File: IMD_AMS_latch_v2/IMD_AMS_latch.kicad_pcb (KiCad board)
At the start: 2 copper layers, 66.9 x 59.9 mm, 43 parts, among them J10 Conn_01x02, J13 Conn_01x02, J2 Conn_01x02, J5 Conn_01x02, J6 Conn_01x02, J7 Conn_01x02, J8 Conn_01x02, J9 Conn_01x02, K1 SANYOU_SRD_Form_C, K2 SANYOU_SRD_Form_C, Q1 AO3400A, Q2 AO3400A, U1 MC14044BDR2G, U2 LM393

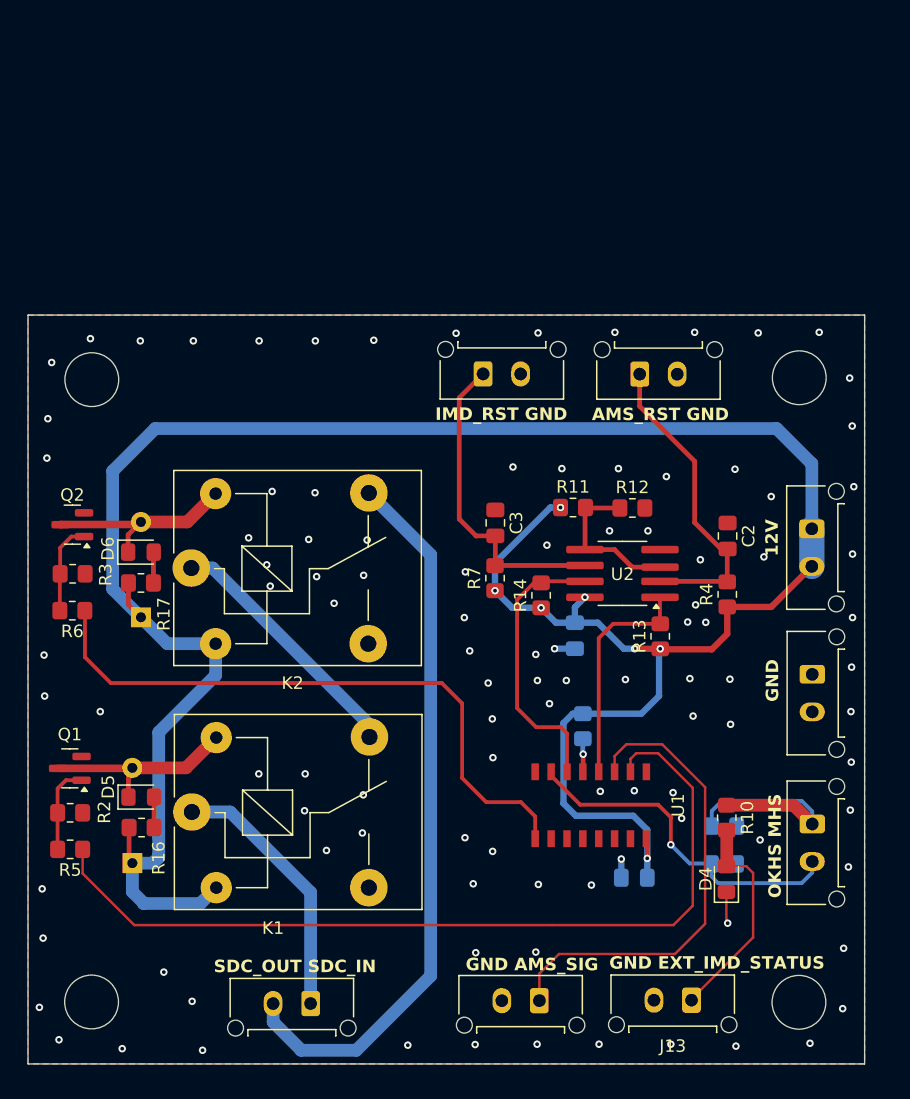
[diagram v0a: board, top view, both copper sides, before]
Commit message: changed to horizontal molex microfit
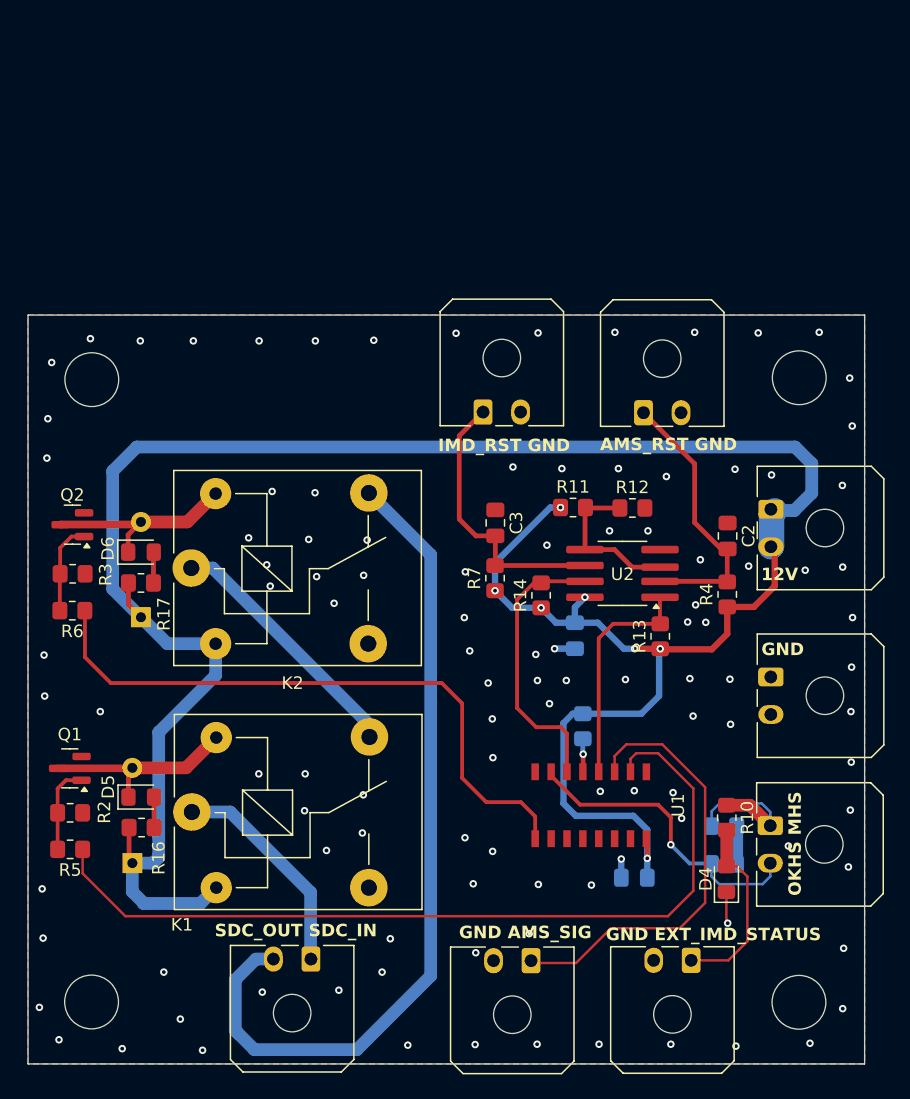
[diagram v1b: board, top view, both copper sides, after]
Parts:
- J10, J13, J2, J5, J6, J7, J8, J9: footprint Connector_Molex:Molex_Micro-Fit_3.0_43650-0215_1x02_P3.00mm_Vertical -> Connector_Molex:Molex_Micro-Fit_3.0_43650-0200_1x02_P3.00mm_Horizontal
- moved J2 3.63 mm to (189.3, 71.2)
- moved J7 3.56 mm to (152.5, 107.2)
- moved J8 3.36 mm to (189.2, 96.5)
- moved J6 3.31 mm to (189.3, 84.7)
- moved J5 3.26 mm to (170.1, 107.3)
- moved J13 3.18 mm to (182.9, 107.3)
- moved J9 3.10 mm to (179.1, 63.5)
- moved J10 3.05 mm to (166.2, 63.5)
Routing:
- net /SDC_OUT: track 58.1 -> 67.9 mm
- net /IMD_MHS: track 18.4 -> 11.9 mm
- net /SDC_IN: track 21.0 -> 17.5 mm
- net /IMD_OKHS: track 27.9 -> 24.6 mm
- net GND: track 5.67 -> 8.71 mm, vias 105 -> 110
- net /AMS_reset_btn: track 25.2 -> 22.3 mm
- net /IMD_reset_btn: track 25.4 -> 22.5 mm
- net /AMS_signal: track 38.3 -> 35.6 mm
- net Net-(D4-A): track 17.5 -> 15.2 mm
- net /AMS_latch: track 69.8 -> 68.6 mm
- net +12V: track 198.3 -> 197.2 mm

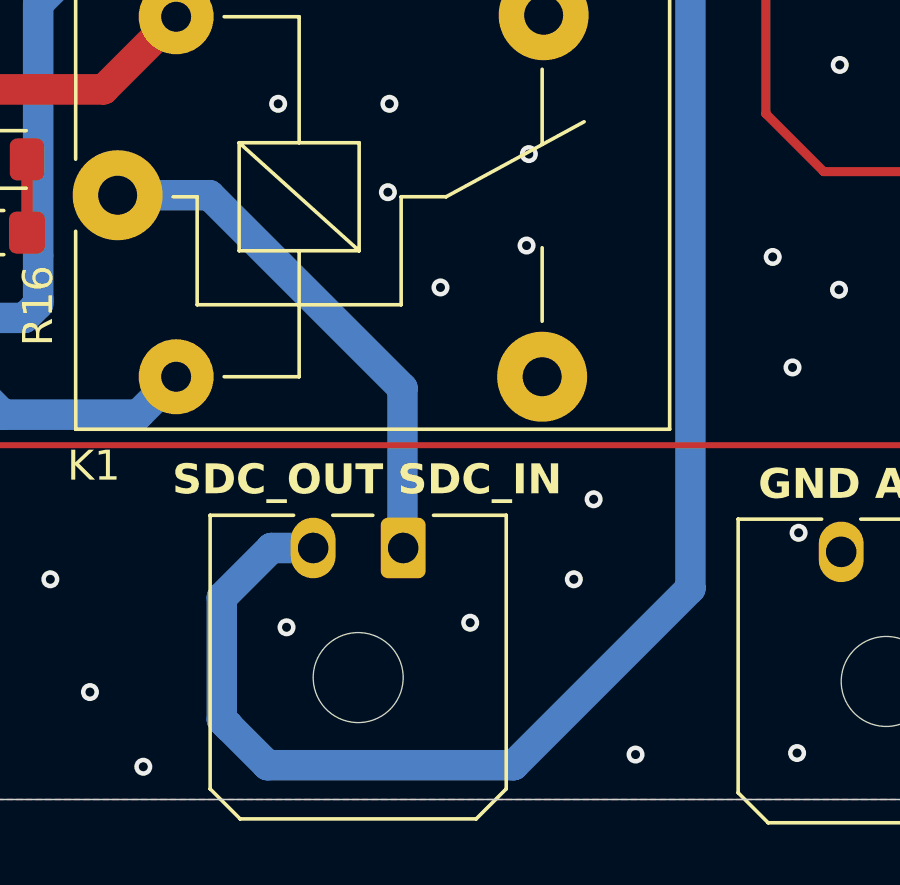
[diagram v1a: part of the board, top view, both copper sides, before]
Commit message: minor update on SDC IN & SDC out wiring
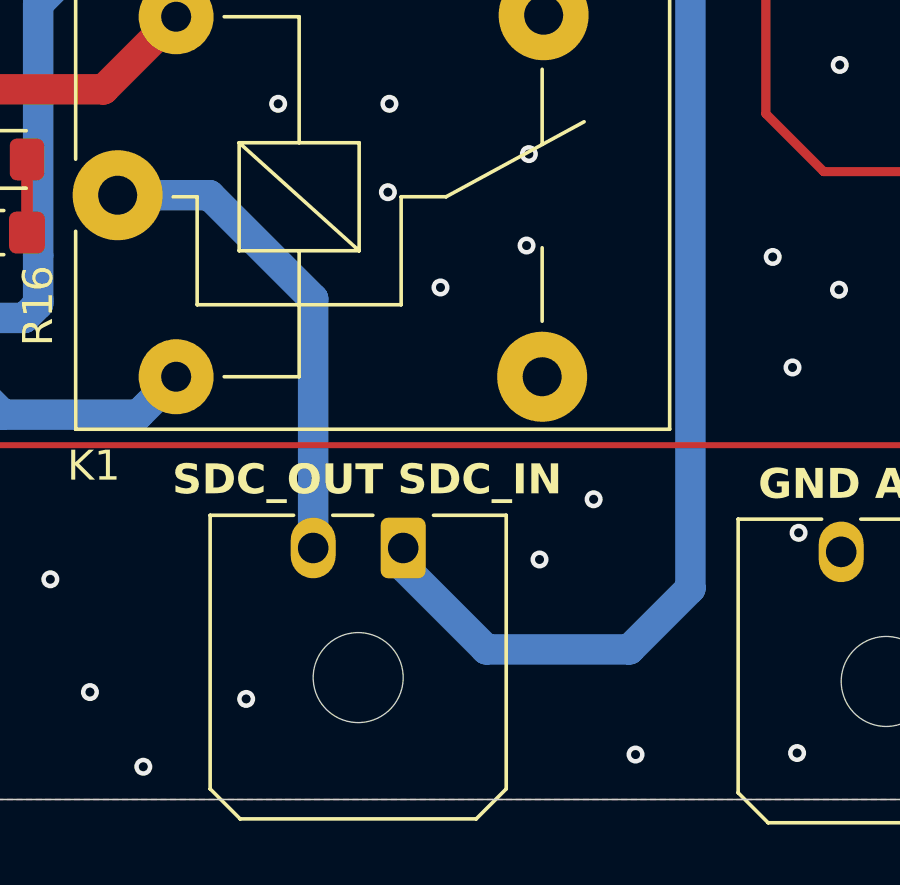
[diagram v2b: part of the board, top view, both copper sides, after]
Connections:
- J7 pad 1: /SDC_IN -> /SDC_OUT
- J7 pad 2: /SDC_OUT -> /SDC_IN
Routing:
- net /SDC_OUT: track 67.9 -> 52.9 mm
- net /SDC_IN: track 17.5 -> 16.9 mm
- net GND: vias 110 -> 109
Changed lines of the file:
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@@
 			(remove_unused_layers no)
 			(roundrect_rratio 0.166667)
-			(net 9 "/SDC_IN")
+			(net 10 "/SDC_OUT")
 			(pinfunction "Pin_1")
 			(pintype "passive")
@@
 			(layers "*.Cu" "*.Mask")
 			(remove_unused_layers no)
-			(net 10 "/SDC_OUT")
+			(net 9 "/SDC_IN")
 			(pinfunction "Pin_2")
 			(pintype "passive")
@@
 	)
 	(via
-		(at 148.59 109.855)
+		(at 147.2438 112.2426)
 		(size 0.6)
 		(drill 0.3)
@@
 	)
 	(via
-		(at 158.1658 108.2548)
+		(at 157.0228 107.5944)
 		(size 0.6)
 		(drill 0.3)
@@
 	)
 	(via
-		(at 154.7114 109.7026)
-		(size 0.6)
-		(drill 0.3)
-		(layers "F.Cu" "B.Cu")
-		(free yes)
-		(net 1)
-	)
-	(via
 		(at 184.0484 80.2894)
 		(size 0.6)
@@
 	)
 	(segment
-		(start 152.503 107.2114)
-		(end 152.4536 107.162)
+		(start 149.4776 98.9062)
+		(end 146.0246 95.4532)
 		(width 1.016)
 		(layer "B.Cu")
@@
 	)
 	(segment
-		(start 152.4536 107.162)
-		(end 152.4536 101.8822)
+		(start 149.4776 107.2114)
+		(end 149.4776 98.9062)
 		(width 1.016)
 		(layer "B.Cu")
@@
 	)
 	(segment
-		(start 152.4536 101.8822)
-		(end 146.0246 95.4532)
-		(width 1.016)
-		(layer "B.Cu")
-		(net 9)
-	)
-	(segment
-		(start 162.052 74.8886)
-		(end 162.052 108.5596)
-		(width 1.016)
-		(layer "B.Cu")
-		(net 10)
-	)
-	(segment
-		(start 148.084 107.2114)
-		(end 149.503 107.2114)
-		(width 1.016)
-		(layer "B.Cu")
-		(net 10)
-	)
-	(segment
-		(start 146.6469 113.1443)
-		(end 146.431 112.9284)
-		(width 1.016)
-		(layer "B.Cu")
-		(net 10)
-	)
-	(segment
 		(start 149.0692 107.6452)
 		(end 149.503 107.2114)
 		(width 0.2)
 		(layer "B.Cu")
-		(net 10)
+		(net 9)
 	)
 	(segment
-		(start 146.431 108.8644)
-		(end 148.084 107.2114)
+		(start 160.02 110.5916)
+		(end 155.249342 110.5916)
 		(width 1.016)
 		(layer "B.Cu")
@@
 	)
 	(segment
-		(start 147.955 114.4524)
-		(end 146.6469 113.1443)
+		(start 155.249342 110.5916)
+		(end 152.4776 107.819858)
 		(width 1.016)
 		(layer "B.Cu")
@@
 	)
 	(segment
-		(start 156.1592 114.4524)
-		(end 147.955 114.4524)
+		(start 152.503 107.2114)
+		(end 152.4536 107.162)
 		(width 1.016)
 		(layer "B.Cu")
@@
 	)
 	(segment
-		(start 157.1094 69.946)
-		(end 162.052 74.8886)
+		(start 162.052 74.8886)
+		(end 162.052 108.5596)
 		(width 1.016)
 		(layer "B.Cu")
@@
 	)
 	(segment
-		(start 146.6469 113.1443)
-		(end 146.558 113.0554)
+		(start 157.1094 69.946)
+		(end 162.052 74.8886)
 		(width 1.016)
 		(layer "B.Cu")
@@
 	)
 	(segment
-		(start 146.431 112.9284)
-		(end 146.431 108.8644)
+		(start 152.4776 107.819858)
+		(end 152.4776 107.2114)
 		(width 1.016)
 		(layer "B.Cu")
@@
 	(segment
 		(start 162.052 108.5596)
-		(end 156.1592 114.4524)
+		(end 160.02 110.5916)
 		(width 1.016)
 		(layer "B.Cu")
@@
 	)
 	(zone
-		(net 14)
-		(net_name "Net-(K1-Pad4)")
+		(net 23)
+		(net_name "Net-(U1-EN)")
 		(layer "B.Cu")
 		(name "$teardrop_padvia$")
 		(hatch full 0.1)
-		(priority 30001)
+		(priority 30002)
 		(attr
 			(teardrop
@@
 		(polygon
 			(pts
-				(xy 144.812131 76.848952) (xy 145.530552 76.130531) (xy 144.213691 75.230765) (xy 142.908693 75.945293)
-				(xy 143.752001 77.176756)
+				(xy 174.4091 90.236164) (xy 174.0281 90.236164) (xy 173.949764 90.771873) (xy 174.244 90.8314) (xy 174.538236 90.771873)
 			)
 		)
 	)
 	(zone
-		(net 23)
-		(net_name "Net-(U1-EN)")
+		(net 14)
+		(net_name "Net-(K1-Pad4)")
 		(layer "B.Cu")
 		(name "$teardrop_padvia$")
 		(hatch full 0.1)
-		(priority 30002)
+		(priority 30001)
 		(attr
 			(teardrop
@@
 		(polygon
 			(pts
-				(xy 174.4091 90.236164) (xy 174.0281 90.236164) (xy 173.949764 90.771873) (xy 174.244 90.8314) (xy 174.538236 90.771873)
+				(xy 144.812131 76.848952) (xy 145.530552 76.130531) (xy 144.213691 75.230765) (xy 142.908693 75.945293)
+				(xy 143.752001 77.176756)
 			)
 		)

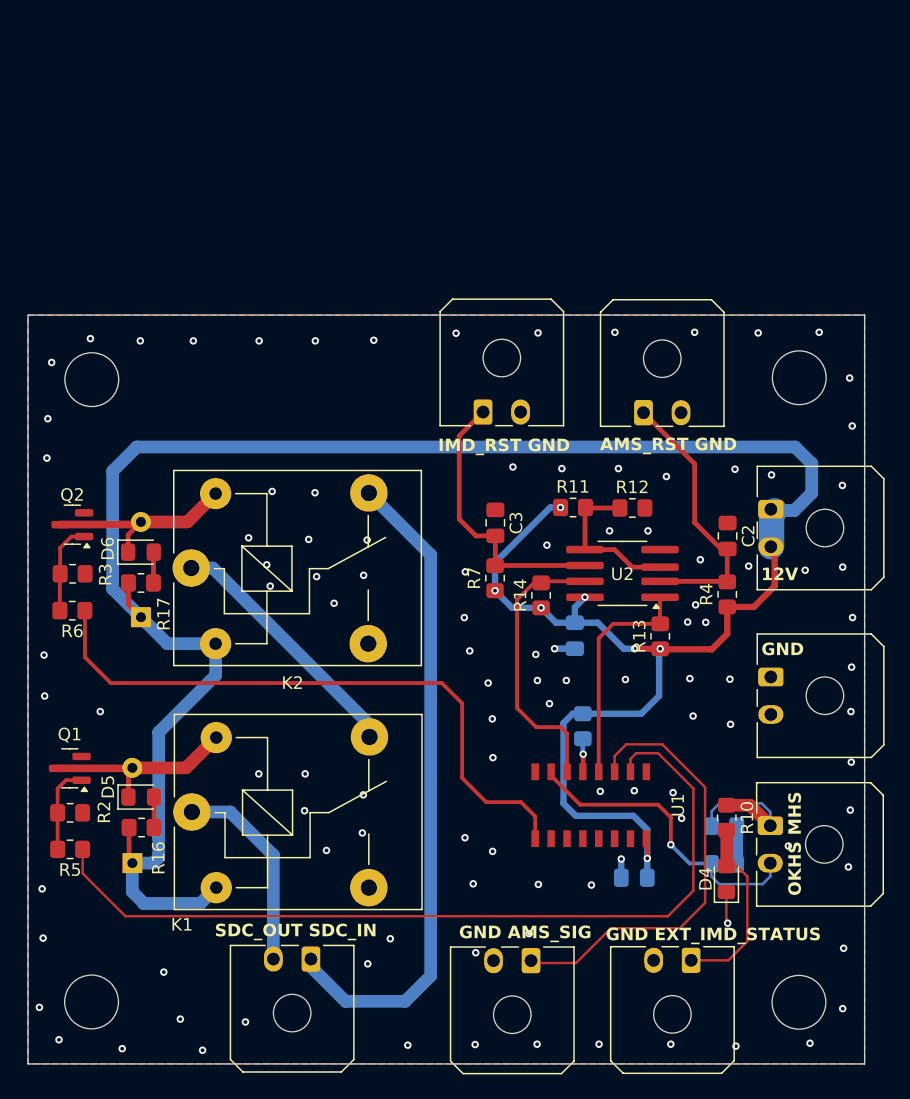
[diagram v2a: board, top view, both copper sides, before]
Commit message: fixed connectors
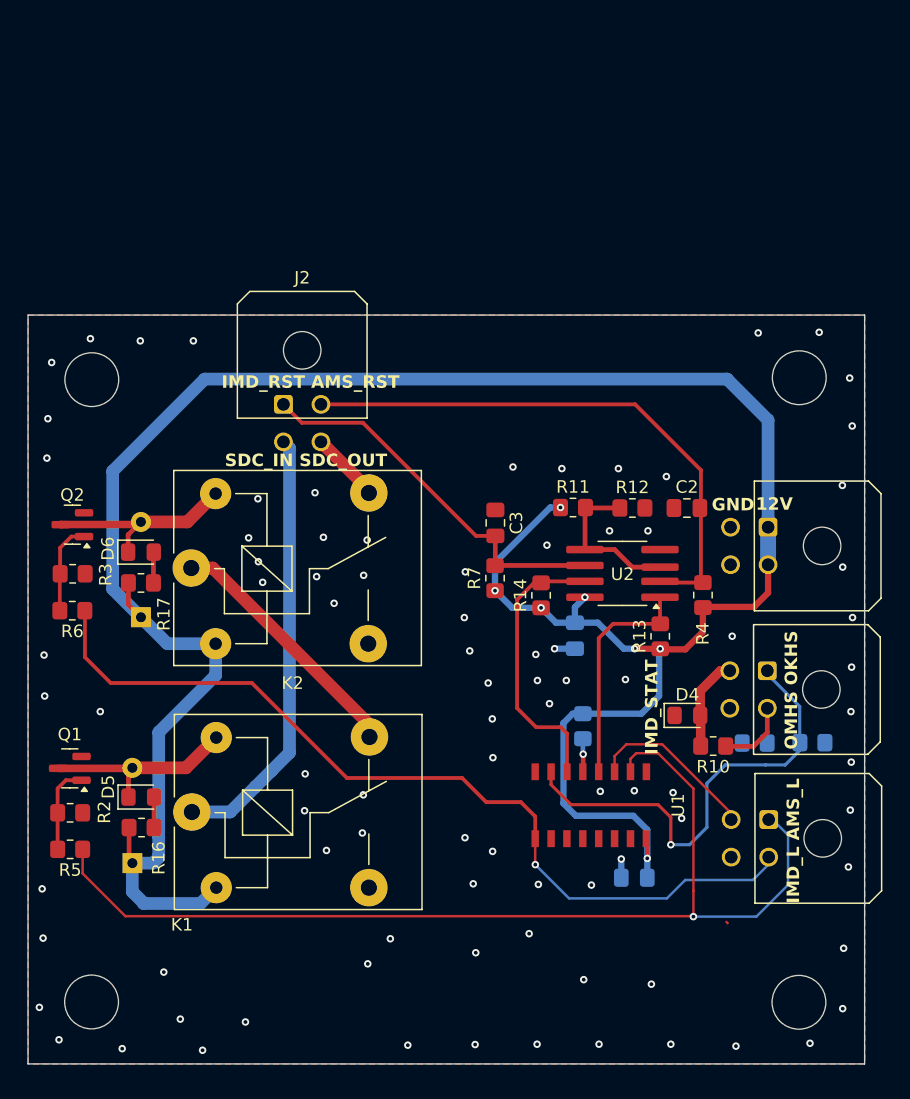
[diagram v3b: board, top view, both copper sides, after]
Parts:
- removed J10, J13, J5, J6, J7, J8, J9: Conn_01x02, Connector_Molex:Molex_Micro-Fit_3.0_43650-0200_1x02_P3.00mm_Horizontal
- added J1: Conn_01x04, Connector_Molex:Molex_Micro-Fit_3.0_43045-0400_2x02_P3.00mm_Horizontal, F.Cu at (189.1, 96.1)
- added J3: Conn_01x04, Connector_Molex:Molex_Micro-Fit_3.0_43045-0400_2x02_P3.00mm_Horizontal, F.Cu at (189.0, 84.2)
- added J4: Conn_01x04, Connector_Molex:Molex_Micro-Fit_3.0_43045-0400_2x02_P3.00mm_Horizontal, F.Cu at (189.0, 72.7)
- J2: value Conn_01x02 -> Conn_01x04; footprint Connector_Molex:Molex_Micro-Fit_3.0_43650-0200_1x02_P3.00mm_Horizontal -> Connector_Molex:Molex_Micro-Fit_3.0_43045-0400_2x02_P3.00mm_Horizontal
- moved J2 39.9 mm to (150.3, 62.9), turned to 0 degrees
- moved D4 13.5 mm to (182.6, 87.7), turned to 0 degrees
- moved R8 12.0 mm to (192.6, 89.9)
- moved R9 7.07 mm to (188.0, 89.9), turned to 180 degrees
- moved R10 5.83 mm to (184.6, 90.2), turned to 180 degrees
- moved C2 3.94 mm to (182.5, 71.2), turned to 0 degrees
- moved R4 1.95 mm to (183.8, 78.1)
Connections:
- net Net-(D4-A) renamed /EXT_LED+
- J2 pad 1: +12V -> /IMD_reset_btn
- J2 pad 2: +12V -> /AMS_reset_btn
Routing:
- net /SDC_OUT: track 52.9 -> 5.42 mm
- net /AMS_reset_btn: track 22.3 -> 45.1 mm
- net /AMS_signal: track 35.6 -> 13.8 mm
- net /IMD_latch: track 49.8 -> 69.8 mm, vias 0 -> 1
- net /SDC_IN: track 16.9 -> 34.8 mm
- net /AMS_latch: track 68.6 -> 85.6 mm, vias 0 -> 1
- net /IMD_OKHS: track 24.6 -> 36.8 mm
- net /IMD_reset_btn: track 22.5 -> 30.9 mm
- net /EXT_LED+: track 15.2 -> 7.45 mm
- net GND: track 8.71 -> 3.27 mm, vias 109 -> 90
- net /IMD_MHS: track 11.9 -> 7.98 mm
- net +12V: track 197.2 -> 197.8 mm
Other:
- board text added: "IMD_L AMS_L"
- board text added: "IMD_RST AMS_RST"
- board text added: "IMD_STAT"
- board text added: "OMHS OKHS"
- board text added: "SDC_IN SDC_OUT"
- board text removed: "AMS_RST GND"
- board text removed: "GND AMS_SIG"
- board text removed: "GND EXT_IMD_STATUS"
- board text removed: "IMD_RST GND"
- board text removed: "OKHS MHS"
- board text removed: "SDC_OUT SDC_IN"

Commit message: fixed connectors
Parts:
- moved J2 26.3 mm to (176.5, 62.5)
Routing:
- net /SDC_IN: track 34.8 -> 60.4 mm
- net /AMS_reset_btn: track 45.1 -> 21.0 mm
- net /SDC_OUT: track 5.42 -> 24.8 mm
- net /IMD_reset_btn: track 30.9 -> 25.9 mm
- net GND: vias 90 -> 99
